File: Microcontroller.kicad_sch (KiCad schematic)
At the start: 21 parts, among them U2 STM32F103C6Tx, Y1 16MHz

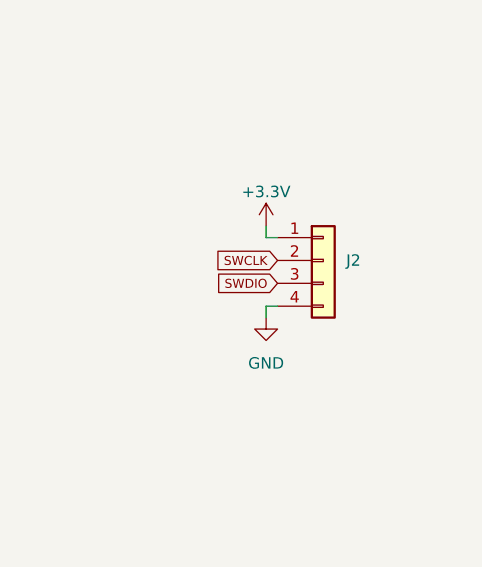
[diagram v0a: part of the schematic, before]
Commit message: 4-layer stackup & some rough component placement
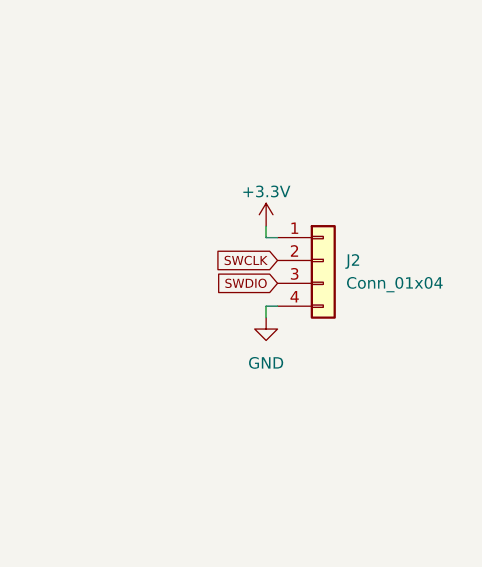
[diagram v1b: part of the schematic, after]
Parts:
- J2: value (none) -> Conn_01x04; footprint (none) -> Connector_PinHeader_2.54mm:PinHeader_1x04_P2.54mm_Vertical
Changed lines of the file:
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@@
       (effects (font (size 1.27 1.27)) (justify left))
     )
-    (property "Value" "" (id 1) (at 224.79 110.4899 0)
+    (property "Value" "Conn_01x04" (id 1) (at 224.79 110.4899 0)
       (effects (font (size 1.27 1.27)) (justify left))
     )
-    (property "Footprint" "" (id 2) (at 222.25 107.95 0)
+    (property "Footprint" "Connector_PinHeader_2.54mm:PinHeader_1x04_P2.54mm_Vertical" (id 2) (at 222.25 107.95 0)
       (effects (font (size 1.27 1.27)) hide)
     )

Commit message: sum layouting
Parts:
- removed RESET1: RST, Button_Switch_THT:SW_PUSH_6mm, symbol Switch:SW_Push
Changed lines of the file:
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@@
   (junction (at 119.38 118.11) (diameter 0) (color 0 0 0 0)
   )
-  (junction (at 161.29 140.97) (diameter 0) (color 0 0 0 0)
-  )
   (junction (at 158.75 39.37) (diameter 0) (color 0 0 0 0)
   )
@@
     (stroke (width 0) (type default) (color 0 0 0 0))
   )
-  (wire (pts (xy 161.29 142.24) (xy 161.29 140.97))
-    (stroke (width 0) (type default) (color 0 0 0 0))
-  )
   (wire (pts (xy 143.51 43.18) (xy 143.51 39.37))
     (stroke (width 0) (type default) (color 0 0 0 0))
   )
-  (wire (pts (xy 161.29 152.4) (xy 161.29 153.67))
-    (stroke (width 0) (type default) (color 0 0 0 0))
-  )
   (wire (pts (xy 153.67 48.26) (xy 153.67 49.53))
     (stroke (width 0) (type default) (color 0 0 0 0))
@@
     (stroke (width 0) (type default) (color 0 0 0 0))
   )
-  (wire (pts (xy 154.94 140.97) (xy 161.29 140.97))
+  (wire (pts (xy 154.94 140.97) (xy 157.48 140.97))
     (stroke (width 0) (type default) (color 0 0 0 0))
   )
@@
     (stroke (width 0) (type default) (color 0 0 0 0))
   )
-  (wire (pts (xy 161.29 140.97) (xy 167.64 140.97))
-    (stroke (width 0) (type default) (color 0 0 0 0))
-  )
   (wire (pts (xy 158.75 43.18) (xy 158.75 39.37))
     (stroke (width 0) (type default) (color 0 0 0 0))
@@
     )
   )
-  (global_label "NRST" (shape input) (at 167.64 140.97 0) (fields_autoplaced)
-    (effects (font (size 1 1)) (justify left))
-    (property "Intersheet References" "${INTERSHEET_REFS}" (id 0) (at 173.3019 140.9075 0)
+  (global_label "NRST" (shape input) (at 157.48 140.97 0) (fields_autoplaced)
+    (effects (font (size 1 1)) (justify left))
+    (property "Intersheet References" "${INTERSHEET_REFS}" (id 0) (at 163.1419 140.9075 0)
       (effects (font (size 1 1)) (justify left) hide)
     )
@@
     )
     (property "Datasheet" "" (id 3) (at 165.1 96.52 0)
-      (effects (font (size 1.27 1.27)) hide)
-    )
-    (pin "1")
-  )
-  (symbol (lib_id "power:GND") (at 161.29 153.67 0) (unit 1)
-    (in_bom yes) (on_board yes) (fields_autoplaced)
-    (property "Reference" "#PWR0127" (id 0) (at 161.29 160.02 0)
-      (effects (font (size 1.27 1.27)) hide)
-    )
-    (property "Value" "GND" (id 1) (at 161.29 158.75 0))
-    (property "Footprint" "" (id 2) (at 161.29 153.67 0)
-      (effects (font (size 1.27 1.27)) hide)
-    )
-    (property "Datasheet" "" (id 3) (at 161.29 153.67 0)
       (effects (font (size 1.27 1.27)) hide)
     )
@@
     (pin "9")
   )
-  (symbol (lib_id "Switch:SW_Push") (at 161.29 147.32 90) (unit 1)
-    (in_bom yes) (on_board yes) (fields_autoplaced)
-    (property "Reference" "RESET1" (id 0) (at 162.56 146.0499 90)
-      (effects (font (size 1.27 1.27)) (justify right))
-    )
-    (property "Value" "RST" (id 1) (at 162.56 148.5899 90)
-      (effects (font (size 1.27 1.27)) (justify right))
-    )
-    (property "Footprint" "Button_Switch_THT:SW_PUSH_6mm" (id 2) (at 156.21 147.32 0)
-      (effects (font (size 1.27 1.27)) hide)
-    )
-    (property "Datasheet" "~" (id 3) (at 156.21 147.32 0)
-      (effects (font (size 1.27 1.27)) hide)
-    )
-    (pin "1")
-    (pin "2")
-  )
   (symbol (lib_id "Device:R_Small") (at 92.71 129.54 0) (unit 1)
